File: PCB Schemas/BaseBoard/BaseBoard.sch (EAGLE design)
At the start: 28 parts, among them IC1 74HC595N, IC2 74HC595N, IC3 74HC595N, Q1 16MHz, U1 ATMEGA2560AU, X1 SQUARE1, X2 SQUARE2, X3 SQUARE3, X4 SQUARE4, X5 53261-05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

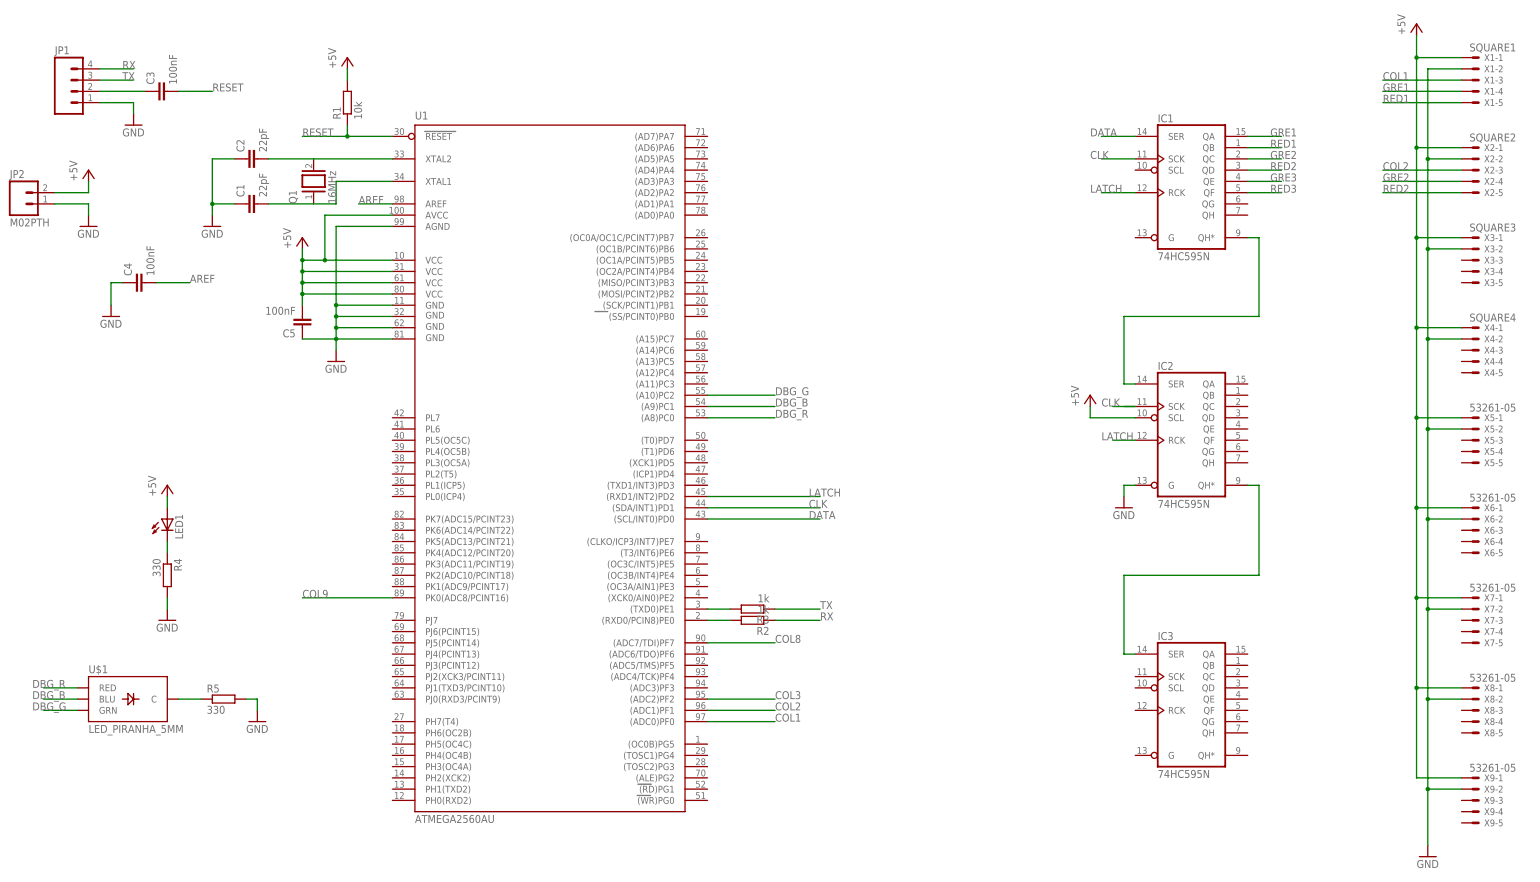
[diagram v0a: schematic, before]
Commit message: completed the schema, still need to add the comm bus
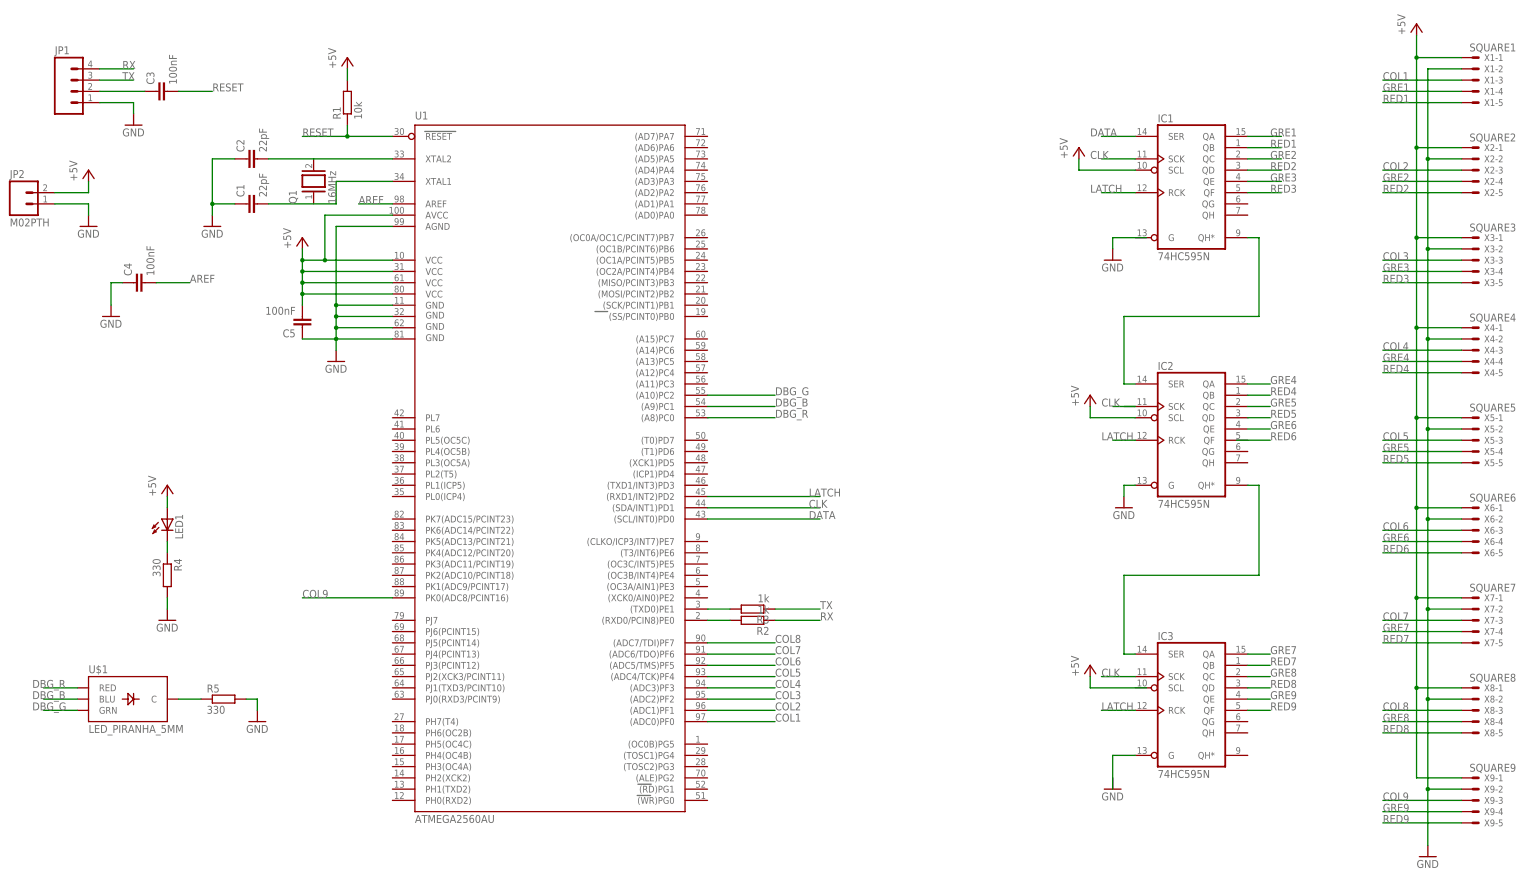
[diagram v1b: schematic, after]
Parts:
- X5: value 53261-05 -> SQUARE5
- X6: value 53261-05 -> SQUARE6
- X7: value 53261-05 -> SQUARE7
- X8: value 53261-05 -> SQUARE8
- X9: value 53261-05 -> SQUARE9
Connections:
- new net COL4: U1.(ADC3)PF3, X4-3.S
- new net COL5: U1.(ADC4/TCK)PF4, X5-3.S
- new net COL6: U1.(ADC5/TMS)PF5, X6-3.S
- new net COL7: U1.(ADC6/TDO)PF6, X7-3.S
- new net GRE4: IC2A.QA, X4-4.S
- new net GRE5: IC2A.QC, X5-4.S
- new net GRE6: IC2A.QE, X6-4.S
- new net GRE7: IC3A.QA, X7-4.S
- new net GRE8: IC3A.QC, X8-4.S
- new net GRE9: IC3A.QE, X9-4.S
- new net N$28: IC3A.G
- new net RED4: IC2A.QB, X4-5.S
- new net RED5: IC2A.QD, X5-5.S
- new net RED6: X6-5.S
- new net RED7: IC3A.QB, X7-5.S
- new net RED8: IC3A.QD, X8-5.S
- new net RED9: IC3A.QF, X9-5.S
- net CLK: now also IC3A.SCK
- net COL3: now also X3-3.S
- net COL8: now also X8-3.S
- net COL9: now also X9-3.S
- net GRE3: now also X3-4.S
- net LATCH: now also IC3A.RCK
- net RED3: now also X3-5.S
- net VCC: now also IC1A.SCL

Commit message: board still needs some work
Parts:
- renumbered U$1 to DEBUG_LED
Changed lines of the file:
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@@
 <part name="GND7" library="supply1" deviceset="GND" device=""/>
 <part name="LED1" library="SparkFun-LED" deviceset="LED" device="3MM"/>
-<part name="U$1" library="SparkFun-LED" deviceset="LED_PIRANHA_5MM" device=""/>
+<part name="DEBUG_LED" library="SparkFun-LED" deviceset="LED_PIRANHA_5MM" device=""/>
 <part name="R4" library="resistor" deviceset="R-EU_" device="0204/7" value="330"/>
 <part name="R5" library="resistor" deviceset="R-EU_" device="0204/7" value="330"/>
@@
 <instance part="GND7" gate="1" x="200.66" y="22.86"/>
 <instance part="LED1" gate="G$1" x="-15.24" y="20.32"/>
-<instance part="U$1" gate="G$1" x="-25.4" y="-20.32"/>
+<instance part="DEBUG_LED" gate="G$1" x="-25.4" y="-20.32"/>
 <instance part="R4" gate="G$1" x="-15.24" y="7.62" rot="R270"/>
 <instance part="R5" gate="G$1" x="-2.54" y="-20.32"/>
@@
 <net name="N$9" class="0">
 <segment>
-<pinref part="U$1" gate="G$1" pin="C"/>
+<pinref part="DEBUG_LED" gate="G$1" pin="C"/>
 <pinref part="R5" gate="G$1" pin="1"/>
 <wire x1="-12.7" y1="-20.32" x2="-7.62" y2="-20.32" width="0.1524" layer="91"/>
@@
 <net name="DBG_R" class="0">
 <segment>
-<pinref part="U$1" gate="G$1" pin="RED"/>
+<pinref part="DEBUG_LED" gate="G$1" pin="RED"/>
 <wire x1="-35.56" y1="-17.78" x2="-43.18" y2="-17.78" width="0.1524" layer="91"/>
 <label x="-45.72" y="-17.78" size="1.778" layer="95"/>
@@
 <net name="DBG_B" class="0">
 <segment>
-<pinref part="U$1" gate="G$1" pin="BLU"/>
+<pinref part="DEBUG_LED" gate="G$1" pin="BLU"/>
 <wire x1="-35.56" y1="-20.32" x2="-43.18" y2="-20.32" width="0.1524" layer="91"/>
 <label x="-45.72" y="-20.32" size="1.778" layer="95"/>
@@
 <net name="DBG_G" class="0">
 <segment>
-<pinref part="U$1" gate="G$1" pin="GRN"/>
+<pinref part="DEBUG_LED" gate="G$1" pin="GRN"/>
 <wire x1="-35.56" y1="-22.86" x2="-43.18" y2="-22.86" width="0.1524" layer="91"/>
 <label x="-45.72" y="-22.86" size="1.778" layer="95"/>

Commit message: changed schema and board
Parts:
- X1: value SQUARE1 -> SQU1
- X2: value SQUARE2 -> SQU2
- X3: value SQUARE3 -> SQU3
- X4: value SQUARE4 -> SQU4
- X5: value SQUARE5 -> SQU5
- X6: value SQUARE6 -> SQU6
- X7: value SQUARE7 -> SQU7
- X8: value SQUARE8 -> SQU8
- X9: value SQUARE9 -> SQU9
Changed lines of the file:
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@@
 <part name="P+3" library="supply1" deviceset="VCC" device="" value="+5V"/>
 <part name="GND5" library="supply1" deviceset="GND" device=""/>
-<part name="X1" library="con-molex" deviceset="53?-05" device="261" value="SQUARE1"/>
-<part name="X2" library="con-molex" deviceset="53?-05" device="261" value="SQUARE2"/>
-<part name="X3" library="con-molex" deviceset="53?-05" device="261" value="SQUARE3"/>
-<part name="X4" library="con-molex" deviceset="53?-05" device="261" value="SQUARE4"/>
-<part name="X5" library="con-molex" deviceset="53?-05" device="261" value="SQUARE5"/>
-<part name="X6" library="con-molex" deviceset="53?-05" device="261" value="SQUARE6"/>
-<part name="X7" library="con-molex" deviceset="53?-05" device="261" value="SQUARE7"/>
-<part name="X8" library="con-molex" deviceset="53?-05" device="261" value="SQUARE8"/>
-<part name="X9" library="con-molex" deviceset="53?-05" device="261" value="SQUARE9"/>
+<part name="X1" library="con-molex" deviceset="53?-05" device="261" value="SQU1"/>
+<part name="X2" library="con-molex" deviceset="53?-05" device="261" value="SQU2"/>
+<part name="X3" library="con-molex" deviceset="53?-05" device="261" value="SQU3"/>
+<part name="X4" library="con-molex" deviceset="53?-05" device="261" value="SQU4"/>
+<part name="X5" library="con-molex" deviceset="53?-05" device="261" value="SQU5"/>
+<part name="X6" library="con-molex" deviceset="53?-05" device="261" value="SQU6"/>
+<part name="X7" library="con-molex" deviceset="53?-05" device="261" value="SQU7"/>
+<part name="X8" library="con-molex" deviceset="53?-05" device="261" value="SQU8"/>
+<part name="X9" library="con-molex" deviceset="53?-05" device="261" value="SQU9"/>
 <part name="P+4" library="supply1" deviceset="VCC" device="" value="+5V"/>
 <part name="GND6" library="supply1" deviceset="GND" device=""/>
